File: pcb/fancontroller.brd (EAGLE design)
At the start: 42.5 x 63.3 mm, 109 parts, among them CN1 USB-MICROB-2TABS, Q1 AO3401, Q10 AO3401, Q11 AO3402, Q12 AO3402, Q13 AO3402, Q14 AO3402, Q15 AO3402, Q16 AO3402, Q17 AO3402, Q18 AO3402, Q2 AO3401, Q3 AO3401, Q4 AO3401, Q5 AO3401, Q6 AO3401, Q7 AO3401, Q8 AO3401, Q9 8M, U1 RT9193, U2 STM32F103-48LQFP

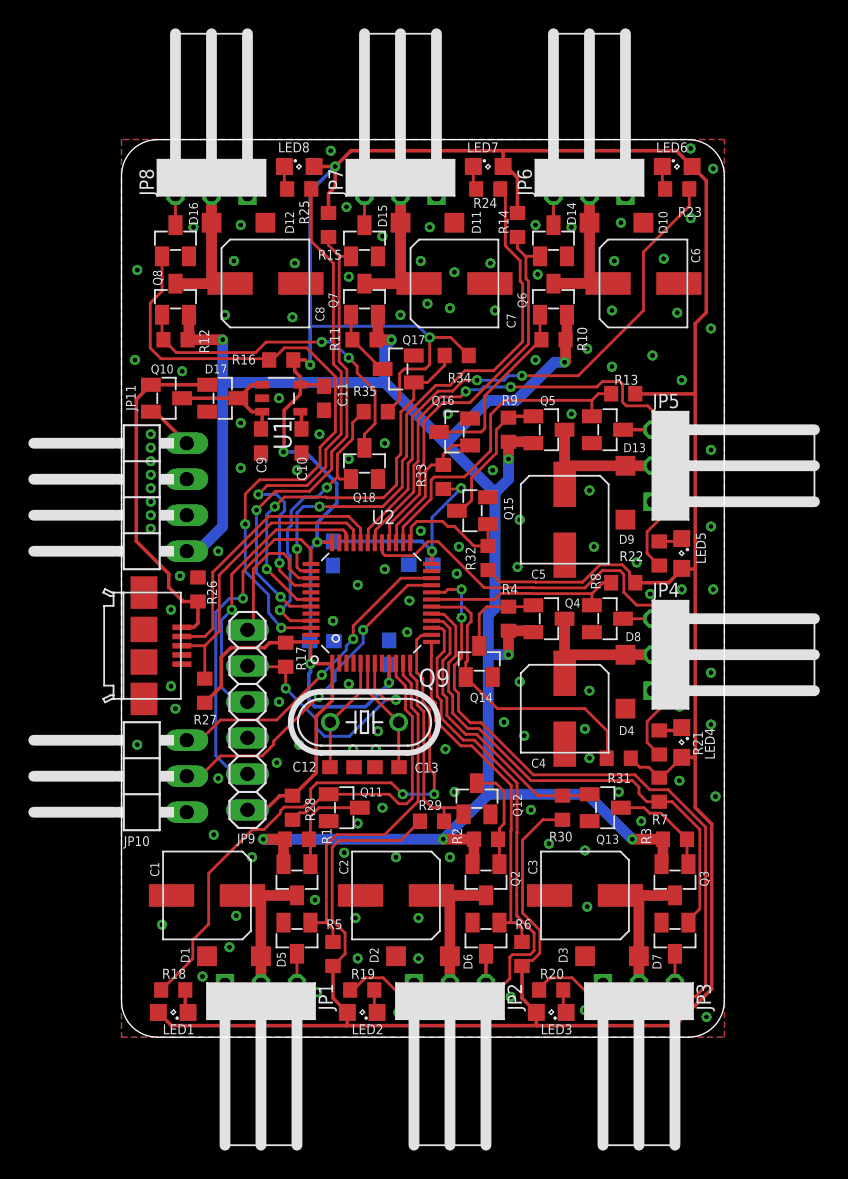
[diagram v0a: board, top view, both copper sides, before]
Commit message: pcb: Connect USB pull-up resistor to GPIO
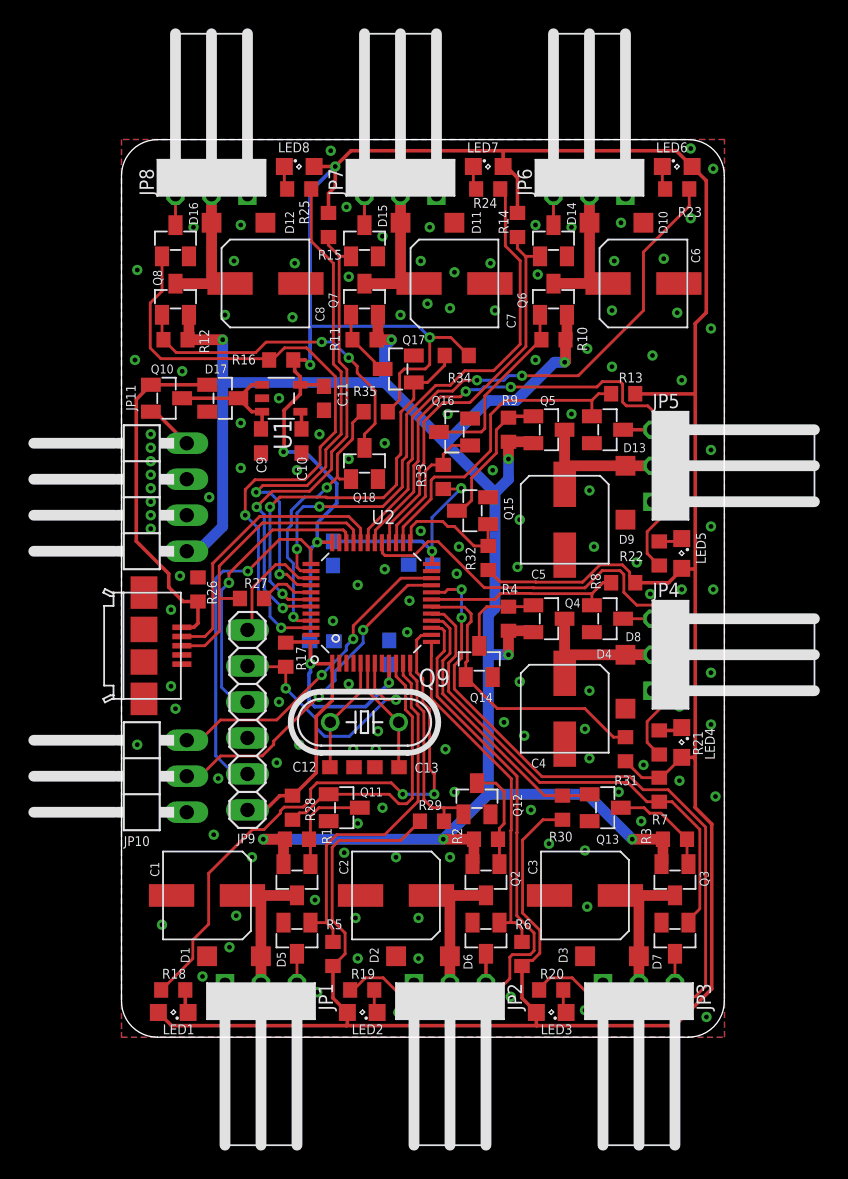
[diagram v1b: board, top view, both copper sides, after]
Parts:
- moved R27 7.31 mm to (9.21, 32.5), turned to 0 degrees
- moved R31 0.79 mm to (35.6, 21.9), turned to 270 degrees
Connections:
- new net USB_PU: R27.2, U2.41
- net +3V3: no longer R27.2
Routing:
- net +3V3: track 323.3 -> 314.9 mm
- net USB_PU: track 0.00 -> 3.97 mm
- net SWO: track 10.1 -> 8.32 mm
- net PWM7: track 21.1 -> 20.1 mm
- net TAC2: track 36.6 -> 35.6 mm
- net PWM2: track 20.6 -> 19.9 mm
- net LED3: track 56.2 -> 55.5 mm
- net TAC6: track 34.0 -> 34.6 mm
- net USB_P: track 21.5 -> 21.0 mm
